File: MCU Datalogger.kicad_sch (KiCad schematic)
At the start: 25 parts, among them U1 24LC1025, U2 24LC1025, U3 DS1337S_, U4 ATMEGA328P-AU, Y1 16 MHz, Y2 32.768kHz

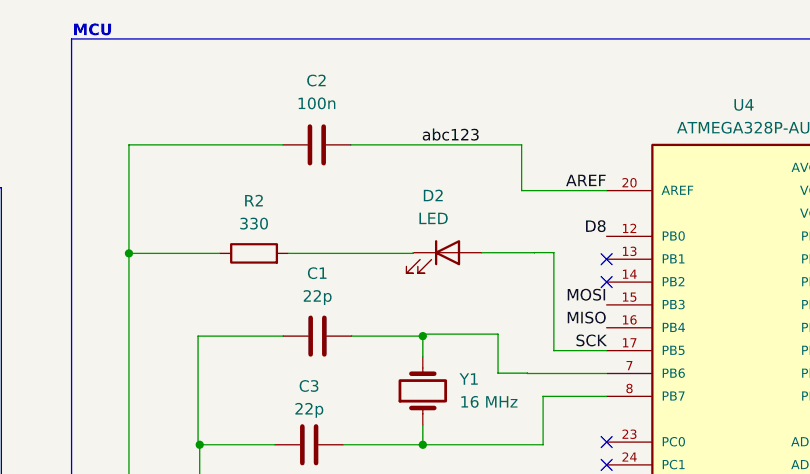
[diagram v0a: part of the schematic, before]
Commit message: Small changes made in schematic, added abc123 label, on branch main
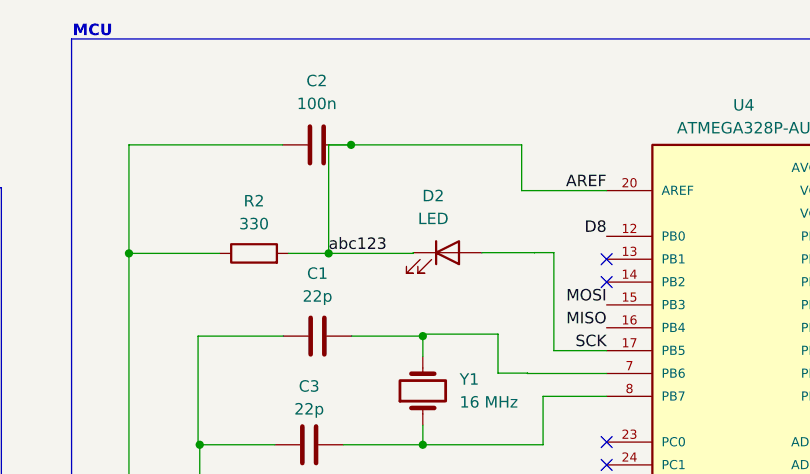
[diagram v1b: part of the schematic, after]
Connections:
- net AREF: now also D2.1 (K), R2.2
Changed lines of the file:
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@@
     (rev "1")
   )
+  (junction (at 168.766 52.1795) (diameter 0) (color 0 0 0 0)
+  )
   (junction (at 104.6347 128.4498) (diameter 0) (color 0 0 0 0)
   )
@@
   )
   (junction (at 154.4415 73.4438) (diameter 0) (color 0 0 0 0)
+  )
+  (junction (at 171.2592 40.1239) (diameter 0) (color 0 0 0 0)
   )
   (junction (at 253.2251 42.666) (diameter 0) (color 0 0 0 0)
@@
     (stroke (width 0) (type default))
   )
-  (wire (pts (xy 190.2111 40.1239) (xy 171.2592 40.1239))
+  (wire (pts (xy 171.2592 40.1239) (xy 190.2111 40.1239))
     (stroke (width 0) (type default))
   )
@@
     (stroke (width 0) (type default))
   )
+  (wire (pts (xy 168.766 52.1795) (xy 168.766 40.1239))
+    (stroke (width 0) (type default))
+  )
   (wire (pts (xy 165.3774 142.7882) (xy 168.4831 142.7882))
     (stroke (width 0) (type default))
@@
     (stroke (width 0) (type default))
   )
+  (wire (pts (xy 168.766 40.1239) (xy 171.2592 40.1239))
+    (stroke (width 0) (type default))
+  )
   (wire (pts (xy 240.7316 70.0072) (xy 240.8066 70.0072))
     (stroke (width 0) (type default))
@@
     (stroke (width 0) (type default))
   )
+  (wire (pts (xy 168.766 52.1795) (xy 178.1691 52.1795))
+    (stroke (width 0) (type default))
+  )
   (wire (pts (xy 168.4831 131.4211) (xy 168.4831 131.6708))
     (stroke (width 0) (type default))
@@
     (stroke (width 0) (type default))
   )
-  (wire (pts (xy 164.2876 52.1795) (xy 178.1691 52.1795))
+  (wire (pts (xy 164.2876 52.1795) (xy 168.766 52.1795))
     (stroke (width 0) (type default))
   )
@@
     (effects (font (size 1.27 1.27)) (justify right bottom))
   )
-  (label "abc123" (at 179.119 40.1239 0) (fields_autoplaced)
-    (effects (font (size 1.27 1.27)) (justify left bottom))
-  )
+  (label "abc123" (at 168.766 52.1795 0) (fields_autoplaced)
+    (effects (font (size 1.27 1.27)) (justify left bottom))
+  )

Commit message: abc123 label fixed
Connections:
- net AREF: no longer D2.1 (K), R2.2
- new net abc123: D2.1 (K), R2.2
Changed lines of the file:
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@@
     (rev "1")
   )
-  (junction (at 168.766 52.1795) (diameter 0) (color 0 0 0 0)
-  )
   (junction (at 104.6347 128.4498) (diameter 0) (color 0 0 0 0)
   )
@@
   )
   (junction (at 154.4415 73.4438) (diameter 0) (color 0 0 0 0)
-  )
-  (junction (at 171.2592 40.1239) (diameter 0) (color 0 0 0 0)
   )
   (junction (at 253.2251 42.666) (diameter 0) (color 0 0 0 0)
@@
     (stroke (width 0) (type default))
   )
-  (wire (pts (xy 168.766 52.1795) (xy 168.766 40.1239))
-    (stroke (width 0) (type default))
-  )
   (wire (pts (xy 165.3774 142.7882) (xy 168.4831 142.7882))
     (stroke (width 0) (type default))
@@
     (stroke (width 0) (type default))
   )
-  (wire (pts (xy 168.766 40.1239) (xy 171.2592 40.1239))
-    (stroke (width 0) (type default))
-  )
   (wire (pts (xy 240.7316 70.0072) (xy 240.8066 70.0072))
     (stroke (width 0) (type default))
@@
     (stroke (width 0) (type default))
   )
-  (wire (pts (xy 168.766 52.1795) (xy 178.1691 52.1795))
-    (stroke (width 0) (type default))
-  )
   (wire (pts (xy 168.4831 131.4211) (xy 168.4831 131.6708))
     (stroke (width 0) (type default))
@@
     (stroke (width 0) (type default))
   )
-  (wire (pts (xy 164.2876 52.1795) (xy 168.766 52.1795))
-    (stroke (width 0) (type default))
-  )
   (wire (pts (xy 261.4417 63.6331) (xy 268.5466 63.6331))
     (stroke (width 0) (type default))
@@
   )
   (wire (pts (xy 179.2296 61.1518) (xy 179.2296 61.3723))
+    (stroke (width 0) (type default))
+  )
+  (wire (pts (xy 164.2876 52.1795) (xy 178.1691 52.1795))
     (stroke (width 0) (type default))
   )
@@
     (effects (font (size 1.27 1.27)) (justify right bottom))
   )
-  (label "abc123" (at 168.766 52.1795 0) (fields_autoplaced)
-    (effects (font (size 1.27 1.27)) (justify left bottom))
-  )
+  (label "abc123" (at 168.9134 52.1795 0) (fields_autoplaced)
+    (effects (font (size 1.27 1.27)) (justify left bottom))
+  )
